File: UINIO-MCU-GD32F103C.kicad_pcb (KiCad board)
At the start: 2 copper layers, 0 parts

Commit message: Finish PCB Layout.
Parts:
- added ?: LOGO, LOGO, F.Cu at (177.3, 100.7)
- added C1: 0.1uF, Capacitor_SMD:C_0402_1005Metric, F.Cu at (138.5, 104.3)
- added C10: 10pF, Capacitor_SMD:C_0402_1005Metric, F.Cu at (145.7, 96.3)
- added C11: 10pF, Capacitor_SMD:C_0402_1005Metric, F.Cu at (145.7, 98.9)
- added C12: 20pF, Capacitor_SMD:C_0402_1005Metric, F.Cu at (143.6, 105.2)
- added C2: 1uF, Capacitor_SMD:C_0402_1005Metric, F.Cu at (175.0, 96.6)
- added C3: 0.1uF, Capacitor_SMD:C_0402_1005Metric, F.Cu at (161.9, 100.8)
- added C4: 0.1uF, Capacitor_SMD:C_0402_1005Metric, F.Cu at (149.4, 105.2)
- added C5: 1uF, Capacitor_SMD:C_0402_1005Metric, F.Cu at (170.2, 96.6)
- added C6: 0.1uF, Capacitor_SMD:C_0402_1005Metric, F.Cu at (161.9, 96.5)
- added C7: 0.1uF, Capacitor_SMD:C_0402_1005Metric, F.Cu at (138.5, 97.2)
- added C8: 20pF, Capacitor_SMD:C_0402_1005Metric, F.Cu at (143.6, 100.8)
- added C9: 0.1uF, Capacitor_SMD:C_0402_1005Metric, F.Cu at (165.8, 104.3)
- added D1: LED_Red, LED_SMD:LED_0603_1608Metric, F.Cu at (173.2, 105.2)
- added HOLE**: Hole-1mm, Uinio:Hole-1mm, F.Cu at (185.2, 109.1)
- added HOLE**: Hole-1mm, Uinio:Hole-1mm, F.Cu at (121.2, 109.1)
- added HOLE**: Hole-1mm, Uinio:Hole-1mm, F.Cu at (121.2, 92.4)
- added HOLE**: Hole-1mm, Uinio:Hole-1mm, F.Cu at (185.2, 92.4)
- added J1: Conn_01x24_Male, Connector_PinHeader_2.54mm:PinHeader_1x24_P2.54mm_Vertical, B.Cu at (182.4, 109.6)
- added J2: Conn_01x24_Male, Connector_PinHeader_2.54mm:PinHeader_1x24_P2.54mm_Vertical, B.Cu at (182.4, 91.9)
- added J3: Conn_01x04_Male, Connector_PinHeader_2.54mm:PinHeader_1x04_P2.54mm_Vertical, F.Cu at (120.8, 104.5)
- added L1: 1KΩ 100Mhz, Inductor_SMD:L_0603_1608Metric, F.Cu at (138.5, 100.7)
- added R1: 2K, Resistor_SMD:R_0402_1005Metric, F.Cu at (172.6, 103.8)
- added R10: 10K, Resistor_SMD:R_0402_1005Metric, F.Cu at (138.5, 98.7)
- added R2: 50R, Resistor_SMD:R_0402_1005Metric, F.Cu at (172.6, 101.1)
- added R3: 50R, Resistor_SMD:R_0402_1005Metric, F.Cu at (172.6, 102.2)
- added R4: 1.5K, Resistor_SMD:R_0402_1005Metric, F.Cu at (172.6, 100.0)
- added R5: 10K, Resistor_SMD:R_0402_1005Metric, F.Cu at (138.5, 102.8)
- added R6: 10K, Resistor_SMD:R_0402_1005Metric, F.Cu at (165.8, 97.1)
- added R7: 1M, Resistor_SMD:R_0402_1005Metric, F.Cu at (145.7, 97.6)
- added R8: 10K, Resistor_SMD:R_0402_1005Metric, F.Cu at (127.1, 102.0)
- added R9: 10K, Resistor_SMD:R_0402_1005Metric, F.Cu at (127.1, 99.4)
- added SW1: BOOT1, Uinio:KEY-SMD_4P-L4.2-W3.4-P2.15-LS4.7, F.Cu at (131.6, 103.6)
- added SW2: NRST, Uinio:KEY-SMD_4P-L4.2-W3.4-P2.15-LS4.7, F.Cu at (165.8, 100.7)
- added SW3: BOOT0, Uinio:KEY-SMD_4P-L4.2-W3.4-P2.15-LS4.7, F.Cu at (131.6, 97.9)
- added U1: ME6211C33M5G-N, Uinio:SOT-23-5_L3.0-W1.7-P0.95-LS2.8-BR, F.Cu at (172.6, 97.0)
- added U2: GD32F103C8T6, Uinio:TQFP-48_L7.0-W7.0-P0.50-LS9.0-BL, F.Cu at (155.1, 100.8)
- added USB1: USB_Type_C_16Pin, Uinio:USB-C-SMD_TYPEC-304J-BCP16, F.Cu at (182.4, 100.7)
- added Y1: 32.768KHz, Uinio:CRYSTAL-FC135-32.768, F.Cu at (143.6, 97.6)
- added Y2: 8MHz, Crystal:Crystal_SMD_3225-4Pin_3.2x2.5mm, F.Cu at (144.8, 103.0)
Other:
- board outline added: 67.4 x 20.3 mm
- board text added: "3V3"
- board text added: "5V"
- board text added: "A0"
- board text added: "A1"
- board text added: "A10"
- board text added: "A11"
- board text added: "A12"
- board text added: "A13"
- board text added: "A14"
- board text added: "A15"
- board text added: "A2"
- board text added: "A3"
- board text added: "A4"
- board text added: "A5"
- board text added: "A6"
- board text added: "A7"
- board text added: "A8"
- board text added: "A9"
- board text added: "B0"
- board text added: "B1"
- board text added: "B10"
- board text added: "B11"
- board text added: "B12"
- board text added: "B13"
- board text added: "B14"
- board text added: "B15"
- board text added: "B2"
- board text added: "B3"
- board text added: "B4"
- board text added: "B5"
- board text added: "B6"
- board text added: "B7"
- board text added: "B8"
- board text added: "B9"
- board text added: "BOOT0"
- board text added: "BOOT1"
- board text added: "C13"
- board text added: "GD32F103Cxxx"
- board text added: "GND"
- board text added: "NRST"
- board text added: "SWCLK"
- board text added: "SWDIO"
- board text added: "VBAT"

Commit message: Finish UINIO-MCU-GD32F103C version 1.0.0.
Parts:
- added ?: LOGO, LOGO, B.Cu at (166.0, 100.9)
- added ?: LOGO, LOGO, B.Cu at (143.6, 100.7)
- added ?: LOGO, LOGO, B.Cu at (171.9, 100.9)
- moved C6 7.03 mm to (155.1, 94.7)
- moved C4 5.85 mm to (155.1, 106.8)
- moved R7 4.96 mm to (147.3, 102.3), turned to -90 degrees
- moved C5 1.22 mm to (170.2, 97.8)
- moved C3 0.63 mm to (161.2, 100.8)
- moved C9 0.55 mm to (165.2, 104.3)
- moved R6 0.53 mm to (165.3, 97.1), turned to 180 degrees
- moved D1 0.46 mm to (172.9, 104.8)
- moved R1 0.37 mm to (172.6, 103.4)
- moved U1 0.32 mm to (172.6, 97.4)
- moved Y2 0.30 mm to (144.8, 102.7)
- moved C12 0.30 mm to (143.6, 104.9)
- moved C8 0.30 mm to (143.6, 100.5)
- moved C2 0.28 mm to (175.0, 96.9)
- turned C11 to 180 degrees
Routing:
- net /VDD_3.3V: track 0.00 -> 149.3 mm, vias 0 -> 5
- net GND: track 0.00 -> 110.2 mm, vias 0 -> 33
- net /PA13/SWDIO: track 0.00 -> 67.1 mm, vias 0 -> 2
- net /PA14/SWCLK: track 0.00 -> 63.3 mm, vias 0 -> 2
- net /NRST: track 0.00 -> 45.0 mm, vias 0 -> 2
- net /PA12: track 0.00 -> 33.3 mm, vias 0 -> 1
- net /PA11: track 0.00 -> 33.1 mm
- net /BOOT0: track 0.00 -> 30.0 mm, vias 0 -> 2
- net /PA3: track 0.00 -> 29.5 mm
- net /PA2: track 0.00 -> 29.5 mm, vias 0 -> 1
- net /PA1: track 0.00 -> 27.2 mm, vias 0 -> 1
- net /PA4: track 0.00 -> 26.4 mm
- net /PA0: track 0.00 -> 25.2 mm, vias 0 -> 1
- net /PA5: track 0.00 -> 24.9 mm
- net /VDD_5V: track 0.00 -> 24.3 mm, vias 0 -> 2
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- added copper zone on B.Cu, net GND
- added copper zone on F.Cu, net GND
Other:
- board text added: "UINIO-MCU-GD32F103C"
- board text added: "Version 1.0.0"

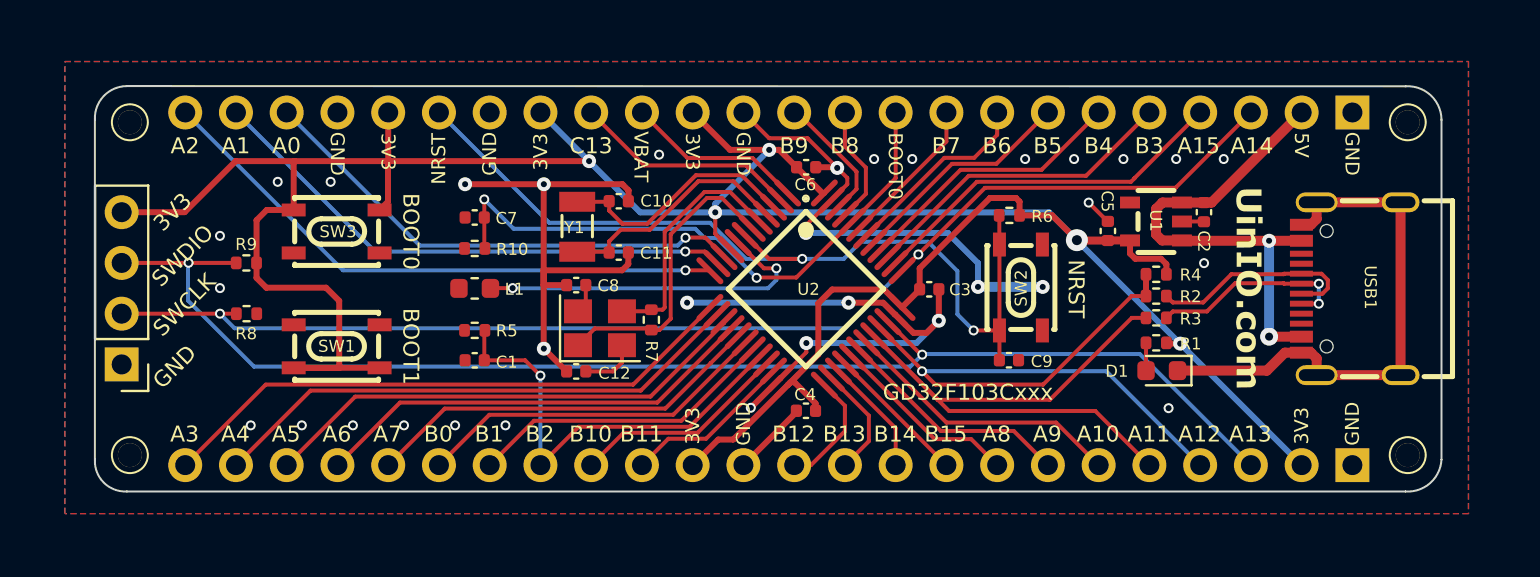
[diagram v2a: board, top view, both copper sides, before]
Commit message: Release UINIO-MCU-GD32F103C version 1.0.0.
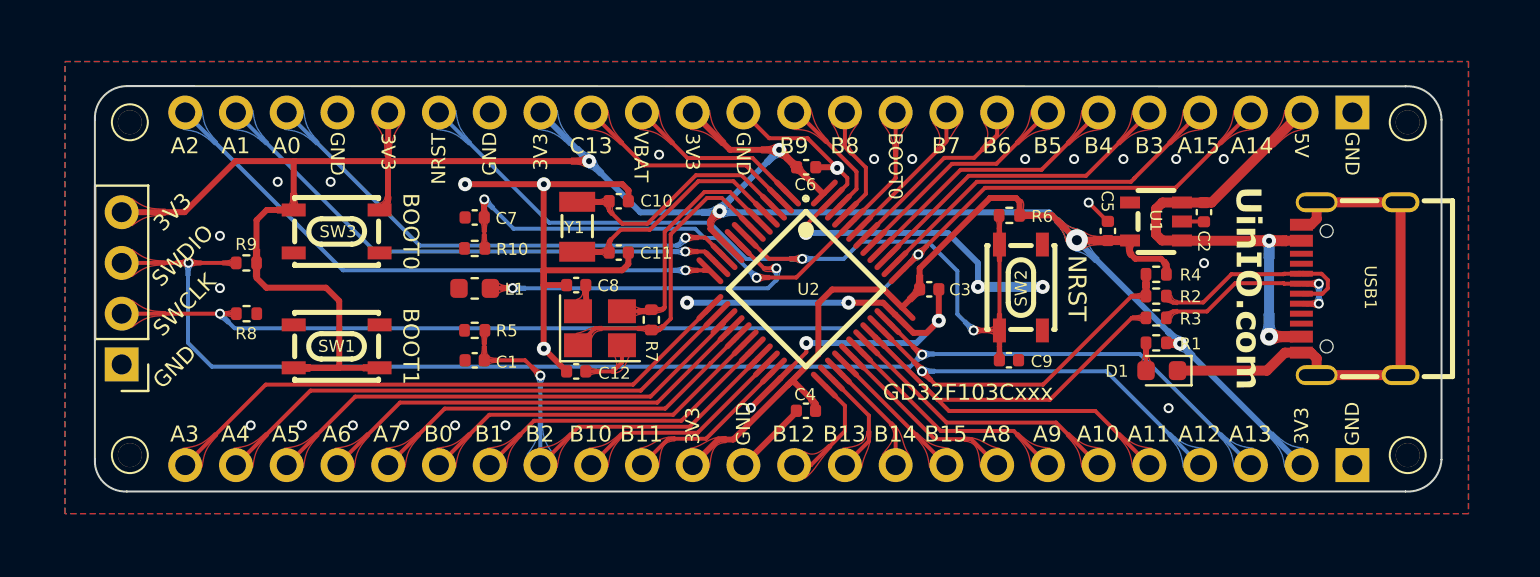
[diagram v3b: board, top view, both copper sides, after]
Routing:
- net /PA13/SWDIO: track 67.1 -> 68.4 mm

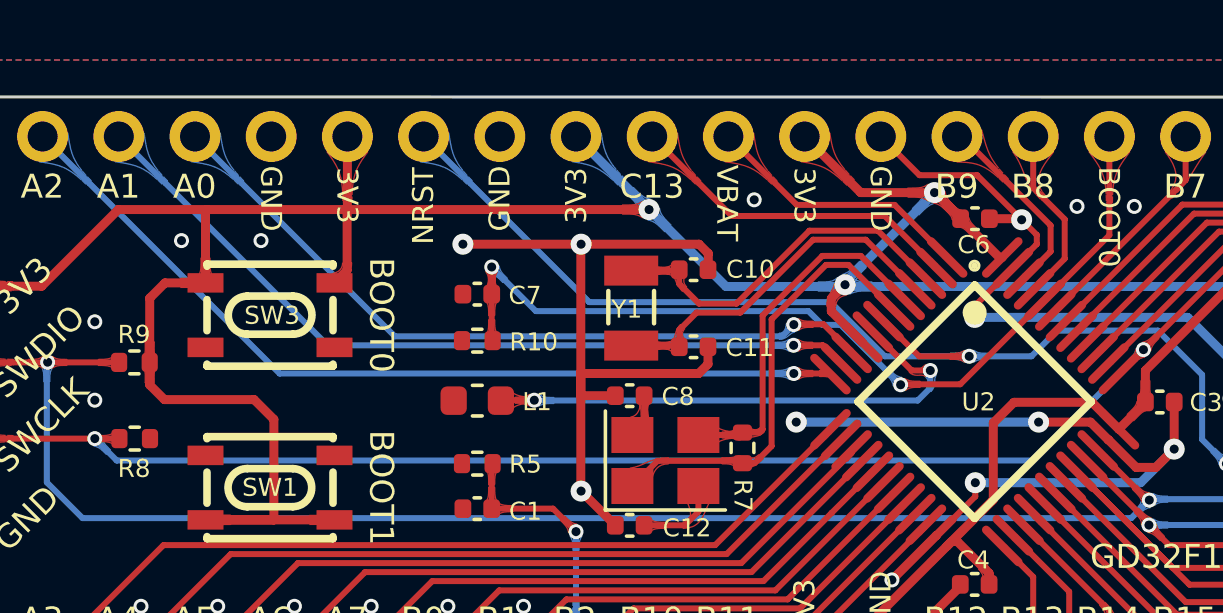
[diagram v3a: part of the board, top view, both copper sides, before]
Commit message: Release UINIO-MCU-GD32F103C version 1.0.0.
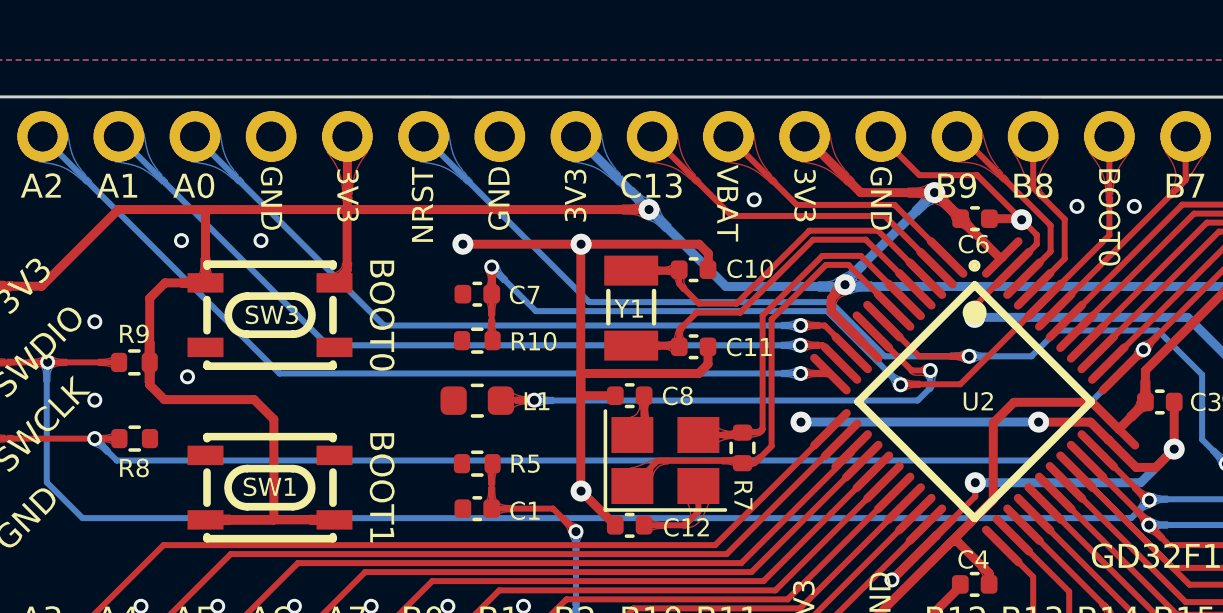
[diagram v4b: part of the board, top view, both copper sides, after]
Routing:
- net GND: track 110.2 -> 110.0 mm, vias 33 -> 34

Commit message: Prepare version 2.0.0.
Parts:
- removed the ? at (177.3, 100.7)
- removed the ? at (166.1, 100.9)
- removed the ? at (143.6, 100.7)
- removed the ? at (171.9, 100.9)
- added ?: LOGO, LOGO, B.Cu at (167.8, 100.7)
- added ?: LOGO, LOGO, B.Cu at (140.6, 100.7)
- J1, J2: value Conn_01x24_Male -> Conn_01x24_Pin
- J3: value Conn_01x04_Male -> Conn_01x04_Pin
- moved HOLE** 0.75 mm to (121.1, 93.1)
- moved HOLE** 0.74 mm to (185.3, 108.3)
- moved HOLE** 0.74 mm to (185.3, 93.1)
- moved HOLE** 0.74 mm to (121.1, 108.3)
- moved USB1 0.72 mm to (183.1, 100.7)
- moved C4 0.12 mm to (155.1, 106.7)
- moved C6 0.09 mm to (155.1, 94.7)
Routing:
- net /VDD_5V: track 24.3 -> 25.8 mm
- net /VDD_3.3V: track 149.7 -> 148.6 mm
- net /USB_Data-: track 10.2 -> 11.1 mm
- net /USB_Data+: track 10.8 -> 11.6 mm
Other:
- board size 67.4 x 20.3 mm -> 68.4 x 20.3 mm
- board text added: "ARM"
- board text added: "GD32F103C/BT6/8T6/6T6/4T6"
- board text added: "UinIO.com"
- board text added: "Version 2.0.0"
- board text removed: "GD32F103Cxxx"
- board text removed: "Version 1.0.0"
